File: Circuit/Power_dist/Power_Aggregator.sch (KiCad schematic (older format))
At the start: 8 parts, among them P16 XT60, P17 XT60, Q6 AUIRFS8409-7P, Q7 AUIRFS8409-7P, U5 LTC4357, U6 LTC4357

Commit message: Merge commit '3eda1dba5ca6e598d51cb20764784284330d387d'
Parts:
- removed F6, F7: FUSE, Zeabus:FUSE_AUTO, symbol Fuse
- added D13, D14, D8: LED_Small, LEDs:LED_0603_HandSoldering, symbol LED_Small
- added R11, R12, R29: 10k, Resistors_SMD:R_0603_HandSoldering, symbol R
- P16, P17: footprint Zeabus:XT60 -> zeabus:XT60
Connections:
- net +VBatt: now also D14.2 (A)
- net GND: now also R11.2, R12.2, R29.2
- net at Q7.S, U6.1 (In): now also P17.1 (P1), D13.2 (A)
- net at Q6.S, U5.1 (In): now also P16.1 (P1), D8.2 (A)
- new net: D8.1 (K), R11.1
- new net: D13.1 (K), R12.1
- new net: D14.1 (K), R29.1
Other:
- moved on the sheet: P16, P17
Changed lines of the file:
@@
 EESchema Schematic File Version 2
+LIBS:Power_Distributor-rescue
 LIBS:power
 LIBS:device
@@
 LIBS:zeabus
 LIBS:ftdi
+LIBS:Power_Distributor-cache
 EELAYER 25 0
 EELAYER END
 $Descr A4 11693 8268
 encoding utf-8
-Sheet 8 9
+Sheet 6 8
 Title "Power Aggregator"
 Date "2017-04-06"
@@
 $EndDescr
 $Comp
-L Fuse F7
-U 1 1 5626464E
-P 4300 4000
-F 0 "F7" H 4400 4050 50  0000 C CNN
-F 1 "FUSE" H 4200 3950 50  0000 C CNN
-F 2 "Zeabus:FUSE_AUTO" H 4300 4000 60  0001 C CNN
-F 3 "" H 4300 4000 60  0000 C CNN
-	1    4300 4000
-	0    1    1    0
-$EndComp
-$Comp
 L XT60 P17
 U 1 1 5626F4F4
-P 3850 4450
-F 0 "P17" H 3850 4600 50  0000 C CNN
-F 1 "XT60" H 3850 4300 50  0000 C CNN
-F 2 "Zeabus:XT60" H 3850 4450 60  0001 C CNN
-F 3 "" H 3850 4450 60  0000 C CNN
-	1    3850 4450
+P 3450 4450
+F 0 "P17" H 3450 4600 50  0000 C CNN
+F 1 "XT60" H 3450 4300 50  0000 C CNN
+F 2 "zeabus:XT60" H 3450 4450 60  0001 C CNN
+F 3 "" H 3450 4450 60  0000 C CNN
+	1    3450 4450
 	-1   0    0    -1
 $EndComp
@@
 $EndComp
 $Comp
-L GND #PWR040
+L GND #PWR030
 U 1 1 5626F752
 P 6350 5250
-F 0 "#PWR040" H 6350 5000 50  0001 C CNN
+F 0 "#PWR030" H 6350 5000 50  0001 C CNN
 F 1 "GND" H 6350 5100 50  0000 C CNN
 F 2 "" H 6350 5250 60  0000 C CNN
@@
 $EndComp
 $Comp
-L GND #PWR041
+L GND #PWR031
 U 1 1 5626F76E
-P 4050 4600
-F 0 "#PWR041" H 4050 4350 50  0001 C CNN
-F 1 "GND" H 4050 4450 50  0000 C CNN
-F 2 "" H 4050 4600 60  0000 C CNN
-F 3 "" H 4050 4600 60  0000 C CNN
-	1    4050 4600
-	1    0    0    -1
-$EndComp
-Wire Wire Line
-	4050 4400 4050 4000
-Wire Wire Line
-	4450 4000 5000 4000
+P 3650 4600
+F 0 "#PWR031" H 3650 4350 50  0001 C CNN
+F 1 "GND" H 3650 4450 50  0000 C CNN
+F 2 "" H 3650 4600 60  0000 C CNN
+F 3 "" H 3650 4600 60  0000 C CNN
+	1    3650 4600
+	1    0    0    -1
+$EndComp
+Wire Wire Line
+	3650 4400 3650 4000
+Wire Wire Line
+	3650 4000 5000 4000
 Wire Wire Line
 	5400 5200 5200 5200
@@
 	6350 5200 6300 5200
 Wire Wire Line
-	4050 4500 4050 4600
-$Comp
-L Fuse F6
-U 1 1 5626F941
-P 4300 2100
-F 0 "F6" H 4400 2150 50  0000 C CNN
-F 1 "FUSE" H 4200 2050 50  0000 C CNN
-F 2 "Zeabus:FUSE_AUTO" H 4300 2100 60  0001 C CNN
-F 3 "" H 4300 2100 60  0000 C CNN
-	1    4300 2100
-	0    1    1    0
-$EndComp
+	3650 4500 3650 4600
 $Comp
 L XT60 P16
 U 1 1 5626F947
-P 3850 2550
-F 0 "P16" H 3850 2700 50  0000 C CNN
-F 1 "XT60" H 3850 2400 50  0000 C CNN
-F 2 "Zeabus:XT60" H 3850 2550 60  0001 C CNN
-F 3 "" H 3850 2550 60  0000 C CNN
-	1    3850 2550
+P 3450 2550
+F 0 "P16" H 3450 2700 50  0000 C CNN
+F 1 "XT60" H 3450 2400 50  0000 C CNN
+F 2 "zeabus:XT60" H 3450 2550 60  0001 C CNN
+F 3 "" H 3450 2550 60  0000 C CNN
+	1    3450 2550
 	-1   0    0    -1
 $EndComp
@@
 $EndComp
 $Comp
-L GND #PWR042
+L GND #PWR032
 U 1 1 5626F959
 P 6350 3350
-F 0 "#PWR042" H 6350 3100 50  0001 C CNN
+F 0 "#PWR032" H 6350 3100 50  0001 C CNN
 F 1 "GND" H 6350 3200 50  0000 C CNN
 F 2 "" H 6350 3350 60  0000 C CNN
@@
 $EndComp
 $Comp
-L GND #PWR043
+L GND #PWR033
 U 1 1 5626F95F
-P 4050 2700
-F 0 "#PWR043" H 4050 2450 50  0001 C CNN
-F 1 "GND" H 4050 2550 50  0000 C CNN
-F 2 "" H 4050 2700 60  0000 C CNN
-F 3 "" H 4050 2700 60  0000 C CNN
-	1    4050 2700
-	1    0    0    -1
-$EndComp
-Wire Wire Line
-	4050 2500 4050 2100
-Wire Wire Line
-	4450 2100 5000 2100
+P 3650 2700
+F 0 "#PWR033" H 3650 2450 50  0001 C CNN
+F 1 "GND" H 3650 2550 50  0000 C CNN
+F 2 "" H 3650 2700 60  0000 C CNN
+F 3 "" H 3650 2700 60  0000 C CNN
+	1    3650 2700
+	1    0    0    -1
+$EndComp
+Wire Wire Line
+	3650 2500 3650 2100
+Wire Wire Line
+	3650 2100 5000 2100
 Wire Wire Line
 	5400 3300 5200 3300
@@
 	6350 3000 6300 3000
 Wire Wire Line
-	5400 2100 6900 2100
+	5400 2100 7700 2100
 Connection ~ 6350 3000
 Wire Wire Line
@@
 	6350 3300 6300 3300
 Wire Wire Line
-	4050 2600 4050 2700
-Text HLabel 6900 2100 2    60   UnSpc ~ 0
+	3650 2600 3650 2700
+Text HLabel 7700 2100 2    60   UnSpc ~ 0
 +VBatt
 Connection ~ 6350 2100
@@
 Connection ~ 6600 2100
 Connection ~ 6350 4000
-Wire Wire Line
-	4050 2100 4150 2100
-Wire Wire Line
-	4050 4000 4150 4000
 NoConn ~ 6300 5100
 NoConn ~ 5400 5000
@@
 NoConn ~ 5400 3200
 NoConn ~ 6300 3200
+$Comp
+L LED_Small D8
+U 1 1 5A394E28
+P 4150 2300
+F 0 "D8" H 4100 2425 50  0000 L CNN
+F 1 "LED_Small" H 3975 2200 50  0000 L CNN
+F 2 "LEDs:LED_0603_HandSoldering" V 4150 2300 50  0001 C CNN
+F 3 "" V 4150 2300 50  0001 C CNN
+	1    4150 2300
+	0    -1   -1   0
+$EndComp
+$Comp
+L R R11
+U 1 1 5A394EA7
+P 4150 2650
+F 0 "R11" V 4230 2650 50  0000 C CNN
+F 1 "10k" V 4150 2650 50  0000 C CNN
+F 2 "Resistors_SMD:R_0603_HandSoldering" V 4080 2650 50  0001 C CNN
+F 3 "" H 4150 2650 50  0001 C CNN
+	1    4150 2650
+	1    0    0    -1
+$EndComp
+$Comp
+L GND #PWR034
+U 1 1 5A394FC4
+P 4150 2950
+F 0 "#PWR034" H 4150 2700 50  0001 C CNN
+F 1 "GND" H 4150 2800 50  0000 C CNN
+F 2 "" H 4150 2950 60  0000 C CNN
+F 3 "" H 4150 2950 60  0000 C CNN
+	1    4150 2950
+	1    0    0    -1
+$EndComp
+Wire Wire Line
+	4150 2200 4150 2100
+Connection ~ 4150 2100
+Wire Wire Line
+	4150 2400 4150 2500
+Wire Wire Line
+	4150 2800 4150 2950
+$Comp
+L LED_Small D13
+U 1 1 5A3951EC
+P 4150 4200
+F 0 "D13" H 4100 4325 50  0000 L CNN
+F 1 "LED_Small" H 3975 4100 50  0000 L CNN
+F 2 "LEDs:LED_0603_HandSoldering" V 4150 4200 50  0001 C CNN
+F 3 "" V 4150 4200 50  0001 C CNN
+	1    4150 4200
+	0    -1   -1   0
+$EndComp
+$Comp
+L R R12
+U 1 1 5A3951F2
+P 4150 4550
+F 0 "R12" V 4230 4550 50  0000 C CNN
+F 1 "10k" V 4150 4550 50  0000 C CNN
+F 2 "Resistors_SMD:R_0603_HandSoldering" V 4080 4550 50  0001 C CNN
+F 3 "" H 4150 4550 50  0001 C CNN
+	1    4150 4550
+	1    0    0    -1
+$EndComp
+$Comp
+L GND #PWR035
+U 1 1 5A3951F8
+P 4150 4850
+F 0 "#PWR035" H 4150 4600 50  0001 C CNN
+F 1 "GND" H 4150 4700 50  0000 C CNN
+F 2 "" H 4150 4850 60  0000 C CNN
+F 3 "" H 4150 4850 60  0000 C CNN
+	1    4150 4850
+	1    0    0    -1
+$EndComp
+Wire Wire Line
+	4150 4300 4150 4400
+Wire Wire Line
+	4150 4700 4150 4850
+$Comp
+L LED_Small D14
+U 1 1 5A397232
+P 7150 2450
+F 0 "D14" H 7100 2575 50  0000 L CNN
+F 1 "LED_Small" H 6975 2350 50  0000 L CNN
+F 2 "LEDs:LED_0603_HandSoldering" V 7150 2450 50  0001 C CNN
+F 3 "" V 7150 2450 50  0001 C CNN
+	1    7150 2450
+	0    -1   -1   0
+$EndComp
+$Comp
+L R R29
+U 1 1 5A397238
+P 7150 2800
+F 0 "R29" V 7230 2800 50  0000 C CNN
+F 1 "10k" V 7150 2800 50  0000 C CNN
+F 2 "Resistors_SMD:R_0603_HandSoldering" V 7080 2800 50  0001 C CNN
+F 3 "" H 7150 2800 50  0001 C CNN
+	1    7150 2800
+	1    0    0    -1
+$EndComp
+$Comp
+L GND #PWR036
+U 1 1 5A39723E
+P 7150 3100
+F 0 "#PWR036" H 7150 2850 50  0001 C CNN
+F 1 "GND" H 7150 2950 50  0000 C CNN
+F 2 "" H 7150 3100 60  0000 C CNN
+F 3 "" H 7150 3100 60  0000 C CNN
+	1    7150 3100
+	1    0    0    -1
+$EndComp
+Wire Wire Line
+	7150 2100 7150 2350
+Wire Wire Line
+	7150 2550 7150 2650
+Wire Wire Line
+	7150 2950 7150 3100
+Connection ~ 7150 2100
+Wire Wire Line
+	4150 4100 4150 4000
+Connection ~ 4150 4000
 $EndSCHEMATC

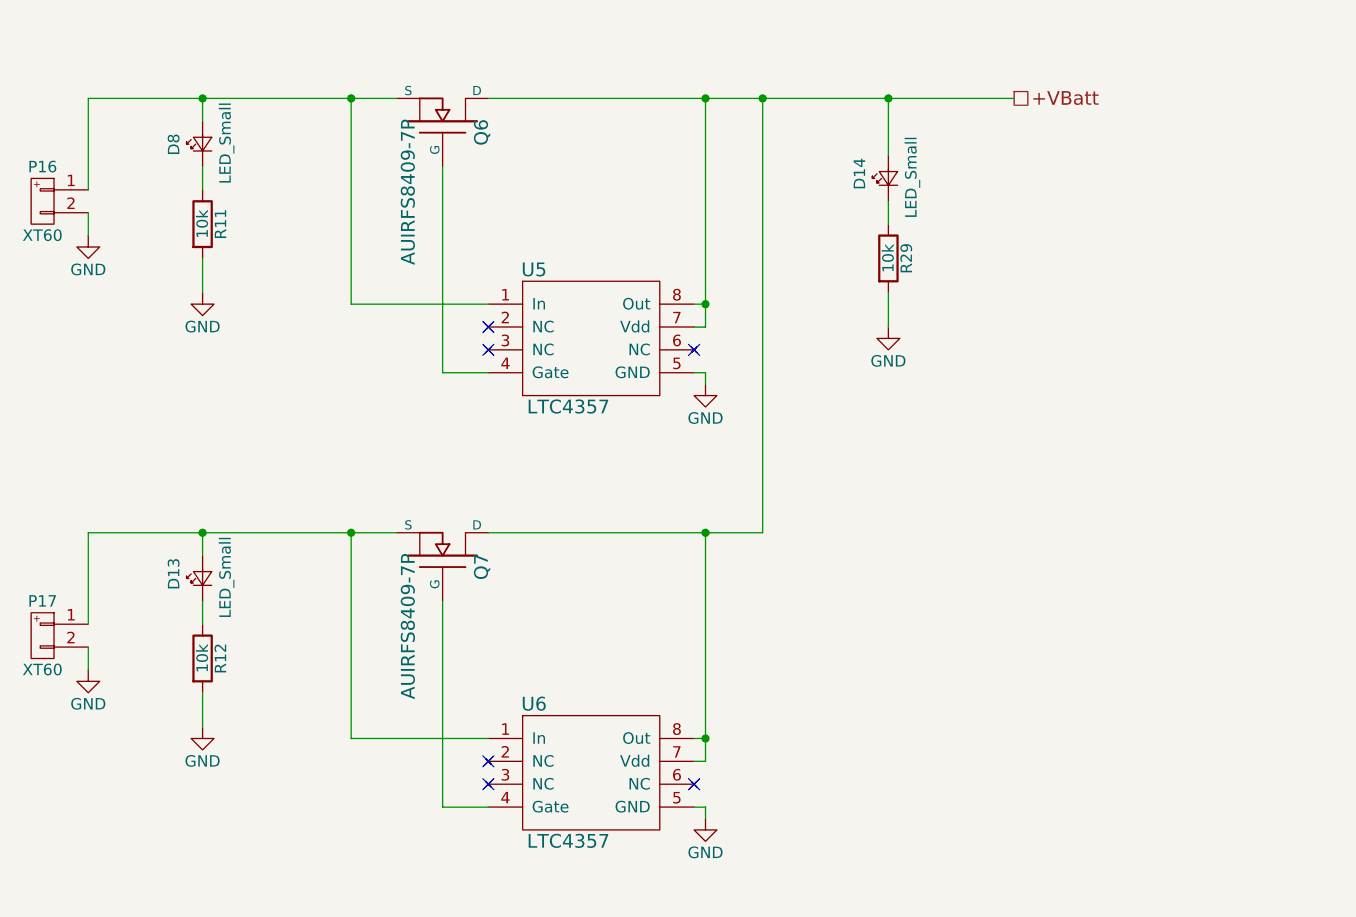
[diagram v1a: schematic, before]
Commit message: adjusted symbol of AUIRFS8409-7P in Power_dist
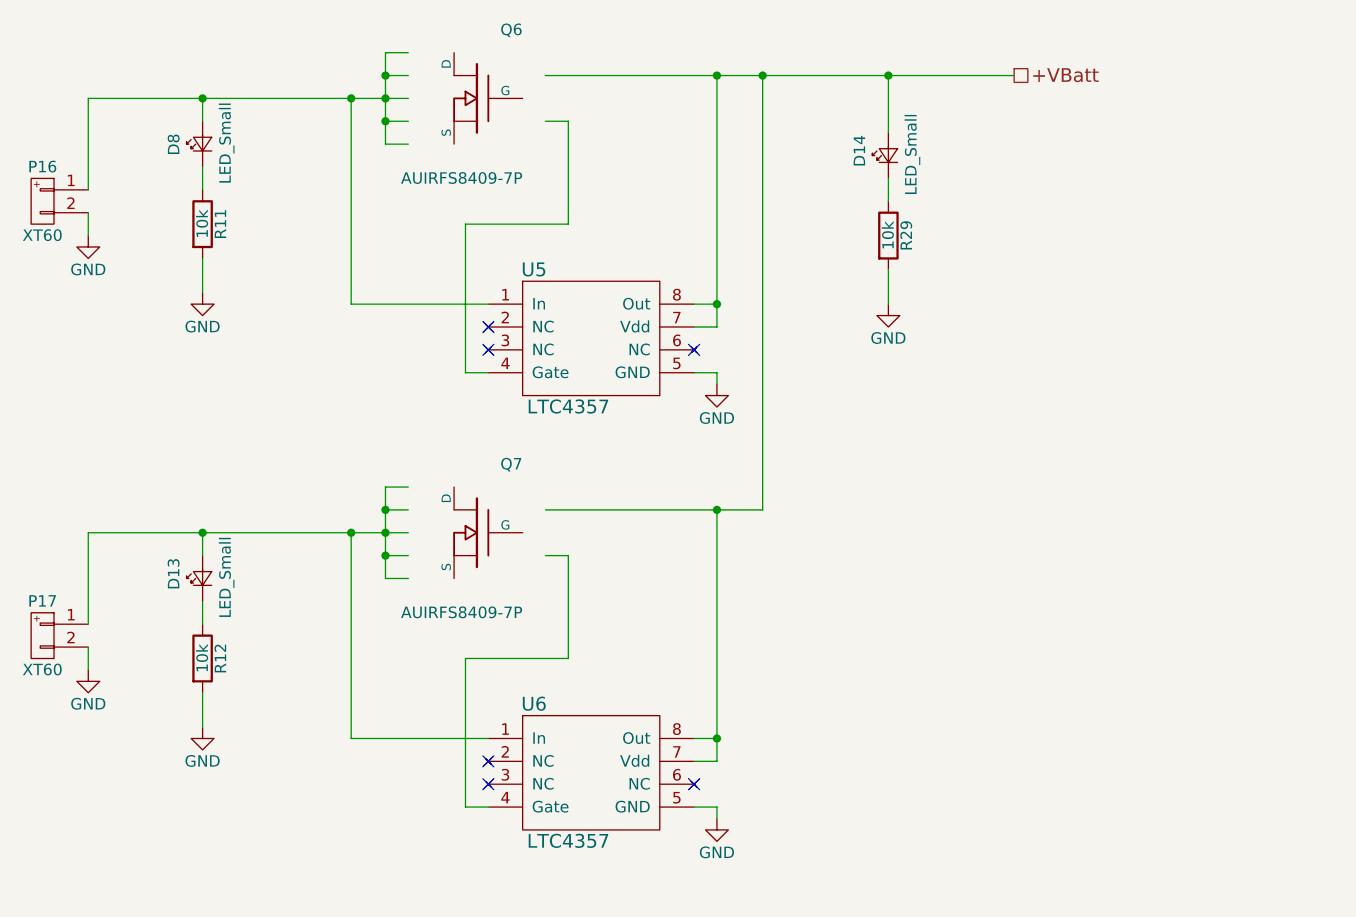
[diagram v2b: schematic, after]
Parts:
- Q6, Q7: footprint Zeabus:D2PAK-7 -> TO_SOT_Packages_SMD:TO-263-6
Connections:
- wire segments 36 -> 52
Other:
- moved on the sheet: D14, R29
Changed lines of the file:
@@
 EESchema Schematic File Version 2
-LIBS:Power_Distributor-rescue
 LIBS:power
 LIBS:device
@@
 LIBS:zeabus
 LIBS:ftdi
-LIBS:Power_Distributor-cache
 EELAYER 25 0
 EELAYER END
@@
 $EndComp
 $Comp
-L AUIRFS8409-7P Q7
-U 1 1 5626F582
-P 5200 4100
-F 0 "Q7" H 5210 4270 60  0000 R CNN
-F 1 "AUIRFS8409-7P" H 5210 3950 60  0000 R CNN
-F 2 "Zeabus:D2PAK-7" H 5200 4100 60  0001 C CNN
-F 3 "" H 5200 4100 60  0000 C CNN
-	1    5200 4100
-	0    1    -1   0
-$EndComp
-$Comp
 L GND #PWR030
 U 1 1 5626F752
-P 6350 5250
-F 0 "#PWR030" H 6350 5000 50  0001 C CNN
-F 1 "GND" H 6350 5100 50  0000 C CNN
-F 2 "" H 6350 5250 60  0000 C CNN
-F 3 "" H 6350 5250 60  0000 C CNN
-	1    6350 5250
+P 6400 5250
+F 0 "#PWR030" H 6400 5000 50  0001 C CNN
+F 1 "GND" H 6400 5100 50  0000 C CNN
+F 2 "" H 6400 5250 60  0000 C CNN
+F 3 "" H 6400 5250 60  0000 C CNN
+	1    6400 5250
 	1    0    0    -1
 $EndComp
@@
 	3650 4400 3650 4000
 Wire Wire Line
-	3650 4000 5000 4000
-Wire Wire Line
-	5400 5200 5200 5200
-Wire Wire Line
-	5200 5200 5200 4300
+	3650 4000 5050 4000
 Wire Wire Line
 	5400 4900 4800 4900
@@
 Connection ~ 4800 4000
 Wire Wire Line
-	6350 5000 6300 5000
-Wire Wire Line
-	6350 4000 6350 5000
-Wire Wire Line
-	6350 4900 6300 4900
-Wire Wire Line
-	5400 4000 6600 4000
-Connection ~ 6350 4900
-Wire Wire Line
-	6350 5250 6350 5200
-Wire Wire Line
-	6350 5200 6300 5200
+	6400 5000 6300 5000
+Wire Wire Line
+	6300 4900 6400 4900
+Wire Wire Line
+	6300 5200 6400 5200
 Wire Wire Line
 	3650 4500 3650 4600
@@
 $EndComp
 $Comp
-L AUIRFS8409-7P Q6
-U 1 1 5626F953
-P 5200 2200
-F 0 "Q6" H 5210 2370 60  0000 R CNN
-F 1 "AUIRFS8409-7P" H 5210 2050 60  0000 R CNN
-F 2 "Zeabus:D2PAK-7" H 5200 2200 60  0001 C CNN
-F 3 "" H 5200 2200 60  0000 C CNN
-	1    5200 2200
-	0    1    -1   0
-$EndComp
-$Comp
 L GND #PWR032
 U 1 1 5626F959
-P 6350 3350
-F 0 "#PWR032" H 6350 3100 50  0001 C CNN
-F 1 "GND" H 6350 3200 50  0000 C CNN
-F 2 "" H 6350 3350 60  0000 C CNN
-F 3 "" H 6350 3350 60  0000 C CNN
-	1    6350 3350
+P 6400 3350
+F 0 "#PWR032" H 6400 3100 50  0001 C CNN
+F 1 "GND" H 6400 3200 50  0000 C CNN
+F 2 "" H 6400 3350 60  0000 C CNN
+F 3 "" H 6400 3350 60  0000 C CNN
+	1    6400 3350
 	1    0    0    -1
 $EndComp
@@
 	3650 2500 3650 2100
 Wire Wire Line
-	3650 2100 5000 2100
-Wire Wire Line
-	5400 3300 5200 3300
-Wire Wire Line
-	5200 3300 5200 2400
+	3650 2100 5050 2100
 Wire Wire Line
 	5400 3000 4800 3000
@@
 Connection ~ 4800 2100
 Wire Wire Line
-	6350 3100 6300 3100
-Wire Wire Line
-	6350 2100 6350 3100
-Wire Wire Line
-	6350 3000 6300 3000
-Wire Wire Line
-	5400 2100 7700 2100
-Connection ~ 6350 3000
-Wire Wire Line
-	6350 3350 6350 3300
-Wire Wire Line
-	6350 3300 6300 3300
-Wire Wire Line
 	3650 2600 3650 2700
-Text HLabel 7700 2100 2    60   UnSpc ~ 0
+Text HLabel 7700 2000 2    60   UnSpc ~ 0
 +VBatt
-Connection ~ 6350 2100
-Wire Wire Line
-	6600 4000 6600 2100
-Connection ~ 6600 2100
-Connection ~ 6350 4000
 NoConn ~ 6300 5100
 NoConn ~ 5400 5000
@@
 L LED_Small D14
 U 1 1 5A397232
-P 7150 2450
-F 0 "D14" H 7100 2575 50  0000 L CNN
-F 1 "LED_Small" H 6975 2350 50  0000 L CNN
-F 2 "LEDs:LED_0603_HandSoldering" V 7150 2450 50  0001 C CNN
-F 3 "" V 7150 2450 50  0001 C CNN
-	1    7150 2450
+P 7150 2350
+F 0 "D14" H 7100 2475 50  0000 L CNN
+F 1 "LED_Small" H 6975 2250 50  0000 L CNN
+F 2 "LEDs:LED_0603_HandSoldering" V 7150 2350 50  0001 C CNN
+F 3 "" V 7150 2350 50  0001 C CNN
+	1    7150 2350
 	0    -1   -1   0
 $EndComp
@@
 L R R29
 U 1 1 5A397238
-P 7150 2800
-F 0 "R29" V 7230 2800 50  0000 C CNN
-F 1 "10k" V 7150 2800 50  0000 C CNN
-F 2 "Resistors_SMD:R_0603_HandSoldering" V 7080 2800 50  0001 C CNN
-F 3 "" H 7150 2800 50  0001 C CNN
-	1    7150 2800
+P 7150 2700
+F 0 "R29" V 7230 2700 50  0000 C CNN
+F 1 "10k" V 7150 2700 50  0000 C CNN
+F 2 "Resistors_SMD:R_0603_HandSoldering" V 7080 2700 50  0001 C CNN
+F 3 "" H 7150 2700 50  0001 C CNN
+	1    7150 2700
 	1    0    0    -1
 $EndComp
@@
 L GND #PWR036
 U 1 1 5A39723E
-P 7150 3100
-F 0 "#PWR036" H 7150 2850 50  0001 C CNN
-F 1 "GND" H 7150 2950 50  0000 C CNN
-F 2 "" H 7150 3100 60  0000 C CNN
-F 3 "" H 7150 3100 60  0000 C CNN
-	1    7150 3100
-	1    0    0    -1
-$EndComp
-Wire Wire Line
-	7150 2100 7150 2350
-Wire Wire Line
-	7150 2550 7150 2650
-Wire Wire Line
-	7150 2950 7150 3100
-Connection ~ 7150 2100
+P 7150 3000
+F 0 "#PWR036" H 7150 2750 50  0001 C CNN
+F 1 "GND" H 7150 2850 50  0000 C CNN
+F 2 "" H 7150 3000 60  0000 C CNN
+F 3 "" H 7150 3000 60  0000 C CNN
+	1    7150 3000
+	1    0    0    -1
+$EndComp
+Wire Wire Line
+	7150 2450 7150 2550
+Wire Wire Line
+	7150 2850 7150 3000
 Wire Wire Line
 	4150 4100 4150 4000
 Connection ~ 4150 4000
+Wire Wire Line
+	5650 2200 5750 2200
+Wire Wire Line
+	5750 2200 5750 2650
+Wire Wire Line
+	5400 3300 5300 3300
+Wire Wire Line
+	5300 3300 5300 2650
+Wire Wire Line
+	5300 2650 5750 2650
+Wire Wire Line
+	4950 1900 4950 2300
+Wire Wire Line
+	4950 2200 5050 2200
+Connection ~ 4950 2100
+Wire Wire Line
+	4950 2300 5050 2300
+Connection ~ 4950 2200
+Wire Wire Line
+	4950 2000 5050 2000
+Wire Wire Line
+	4950 1900 5050 1900
+Connection ~ 4950 2000
+Wire Wire Line
+	5650 2000 7700 2000
+Wire Wire Line
+	7150 2250 7150 2000
+Connection ~ 7150 2000
+Wire Wire Line
+	6300 3100 6400 3100
+Wire Wire Line
+	6400 3100 6400 2000
+Connection ~ 6400 2000
+Connection ~ 6400 3000
+Wire Wire Line
+	6300 3000 6400 3000
+Wire Wire Line
+	6300 3300 6400 3300
+Wire Wire Line
+	6400 3300 6400 3350
+Wire Wire Line
+	6400 5200 6400 5250
+Wire Wire Line
+	5050 3900 4950 3900
+Wire Wire Line
+	4950 3800 4950 4200
+Connection ~ 4950 4000
+Wire Wire Line
+	4950 3800 5050 3800
+Connection ~ 4950 3900
+Wire Wire Line
+	4950 4100 5050 4100
+Wire Wire Line
+	4950 4200 5050 4200
+Connection ~ 4950 4100
+Wire Wire Line
+	5650 3900 6600 3900
+Wire Wire Line
+	6600 3900 6600 2000
+Connection ~ 6600 2000
+Wire Wire Line
+	6400 3900 6400 5000
+Connection ~ 6400 3900
+Connection ~ 6400 4900
+Wire Wire Line
+	5650 4100 5750 4100
+Wire Wire Line
+	5750 4100 5750 4550
+Wire Wire Line
+	5750 4550 5300 4550
+Wire Wire Line
+	5300 4550 5300 5200
+Wire Wire Line
+	5300 5200 5400 5200
+$Comp
+L AUIRFS8409-7P Q7
+U 1 1 5B464942
+P 5350 4000
+F 0 "Q7" H 5150 4300 50  0000 L CNN
+F 1 "AUIRFS8409-7P" H 5150 3650 50  0000 L CNN
+F 2 "TO_SOT_Packages_SMD:TO-263-6" H 5350 3550 50  0001 C CIN
+F 3 "" H 5150 4300 50  0001 L CNN
+	1    5350 4000
+	-1   0    0    -1
+$EndComp
+$Comp
+L AUIRFS8409-7P Q6
+U 1 1 5B465336
+P 5350 2100
+F 0 "Q6" H 5150 2400 50  0000 L CNN
+F 1 "AUIRFS8409-7P" H 5150 1750 50  0000 L CNN
+F 2 "TO_SOT_Packages_SMD:TO-263-6" H 5350 1650 50  0001 C CIN
+F 3 "" H 5150 2400 50  0001 L CNN
+	1    5350 2100
+	-1   0    0    -1
+$EndComp
 $EndSCHEMATC

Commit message: added inductive spikes protection at power_aggregator of Power_dist
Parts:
- added C? (x2): 1uF, Capacitors_SMD:C_0603_HandSoldering, symbol C_Small
- added C?: 47uF, Capacitors_SMD:CP_Elec_6.3x5.8, symbol C_Small
- added D? (x2): B340AE, Diodes_SMD:D_SMA_Handsoldering, symbol D
- added R? (x2): 100, Resistors_SMD:R_0603_HandSoldering, symbol R
- D13: value LED_Small -> BATT2_LED
- D14: value LED_Small -> BATT_LED
- D8: value LED_Small -> BATT1_LED
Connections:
- wire segments 52 -> 66
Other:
- moved on the sheet: D13, D14, D8, Q6, Q7, R12, R29, U5, U6
